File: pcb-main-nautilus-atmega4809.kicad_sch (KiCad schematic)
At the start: 11 parts, among them J1 694106301002, J2 105017-0001, J3 FTSH-105-01-L-DV-007-K, J4 AVR-UPDI-6, J5 Conn_01x06, J6 Conn_01x10, J7 Conn_01x08, J8 Conn_01x08

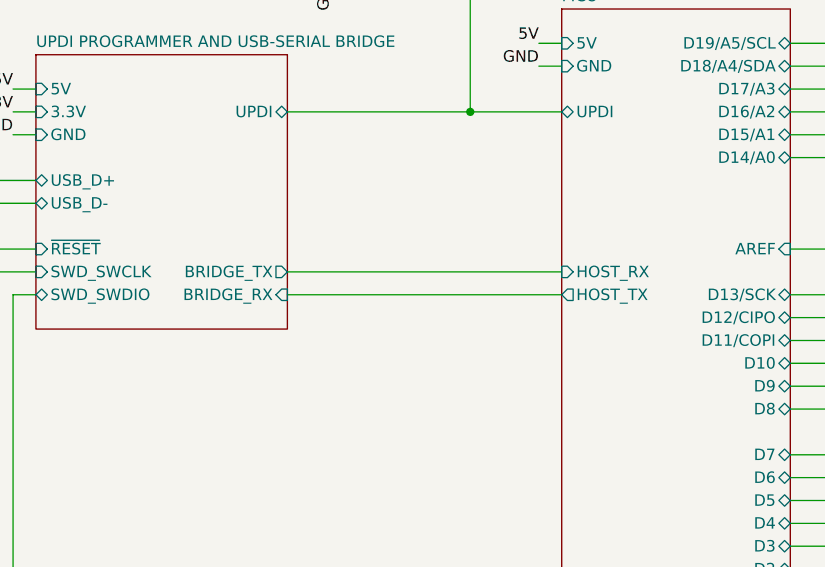
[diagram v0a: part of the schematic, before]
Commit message: Rename serial signals
Supports #2.
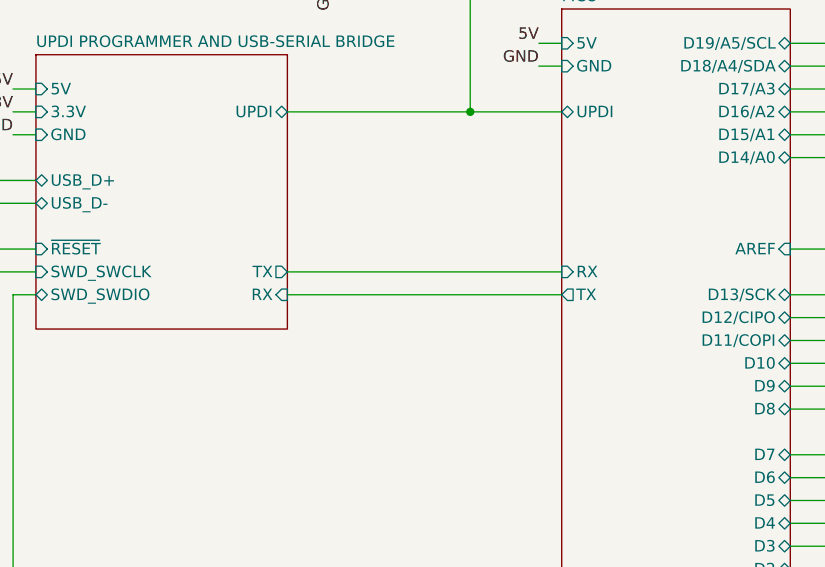
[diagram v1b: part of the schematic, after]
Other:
- sheet MCU ports: added RX, TX; removed HOST_RX, HOST_TX
- sheet UPDI PROGRAMMER AND USB-SERIAL BRIDGE ports: added RX, TX; removed BRIDGE_RX, BRIDGE_TX
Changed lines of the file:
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@@
       (effects (font (size 1.27 1.27)) (justify left))
     )
-    (pin "HOST_RX" input (at 177.8 96.52 180)
+    (pin "RX" input (at 177.8 96.52 180)
       (effects (font (size 1.27 1.27)) (justify left))
     )
-    (pin "HOST_TX" output (at 177.8 99.06 180)
+    (pin "TX" output (at 177.8 99.06 180)
       (effects (font (size 1.27 1.27)) (justify left))
     )
@@
       (effects (font (size 1.27 1.27)) (justify left))
     )
-    (pin "BRIDGE_RX" input (at 147.32 99.06 0)
+    (pin "RX" input (at 147.32 99.06 0)
       (effects (font (size 1.27 1.27)) (justify right))
     )
-    (pin "BRIDGE_TX" output (at 147.32 96.52 0)
+    (pin "TX" output (at 147.32 96.52 0)
       (effects (font (size 1.27 1.27)) (justify right))
     )

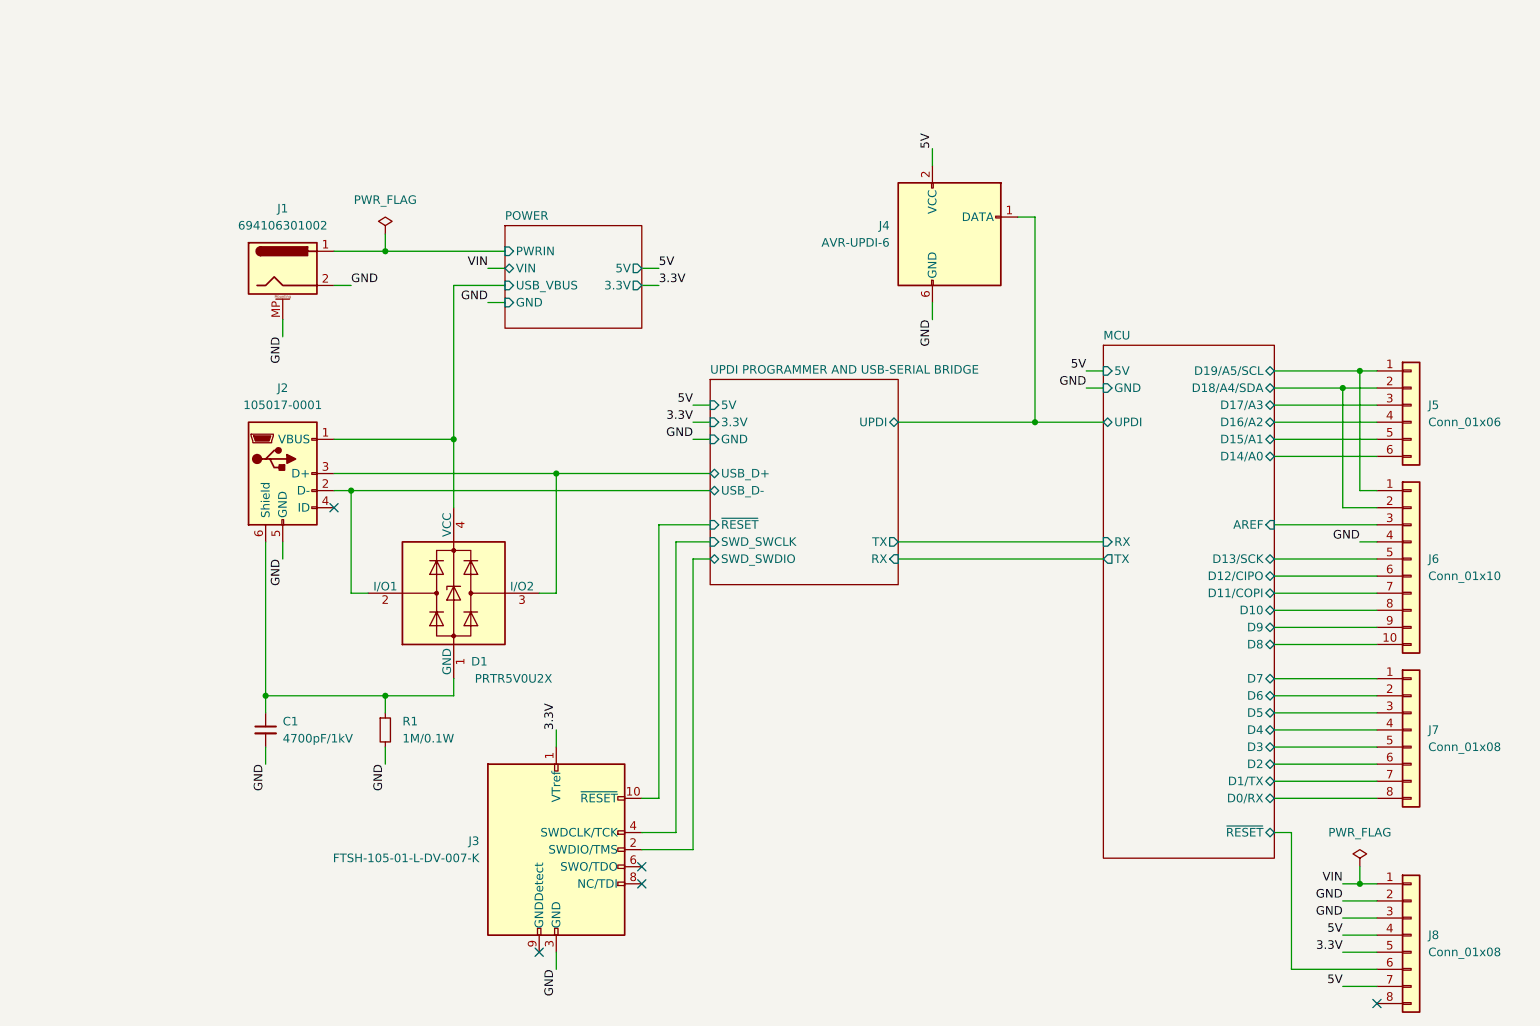
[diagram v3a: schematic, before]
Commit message: Update BOM
Supports #2.
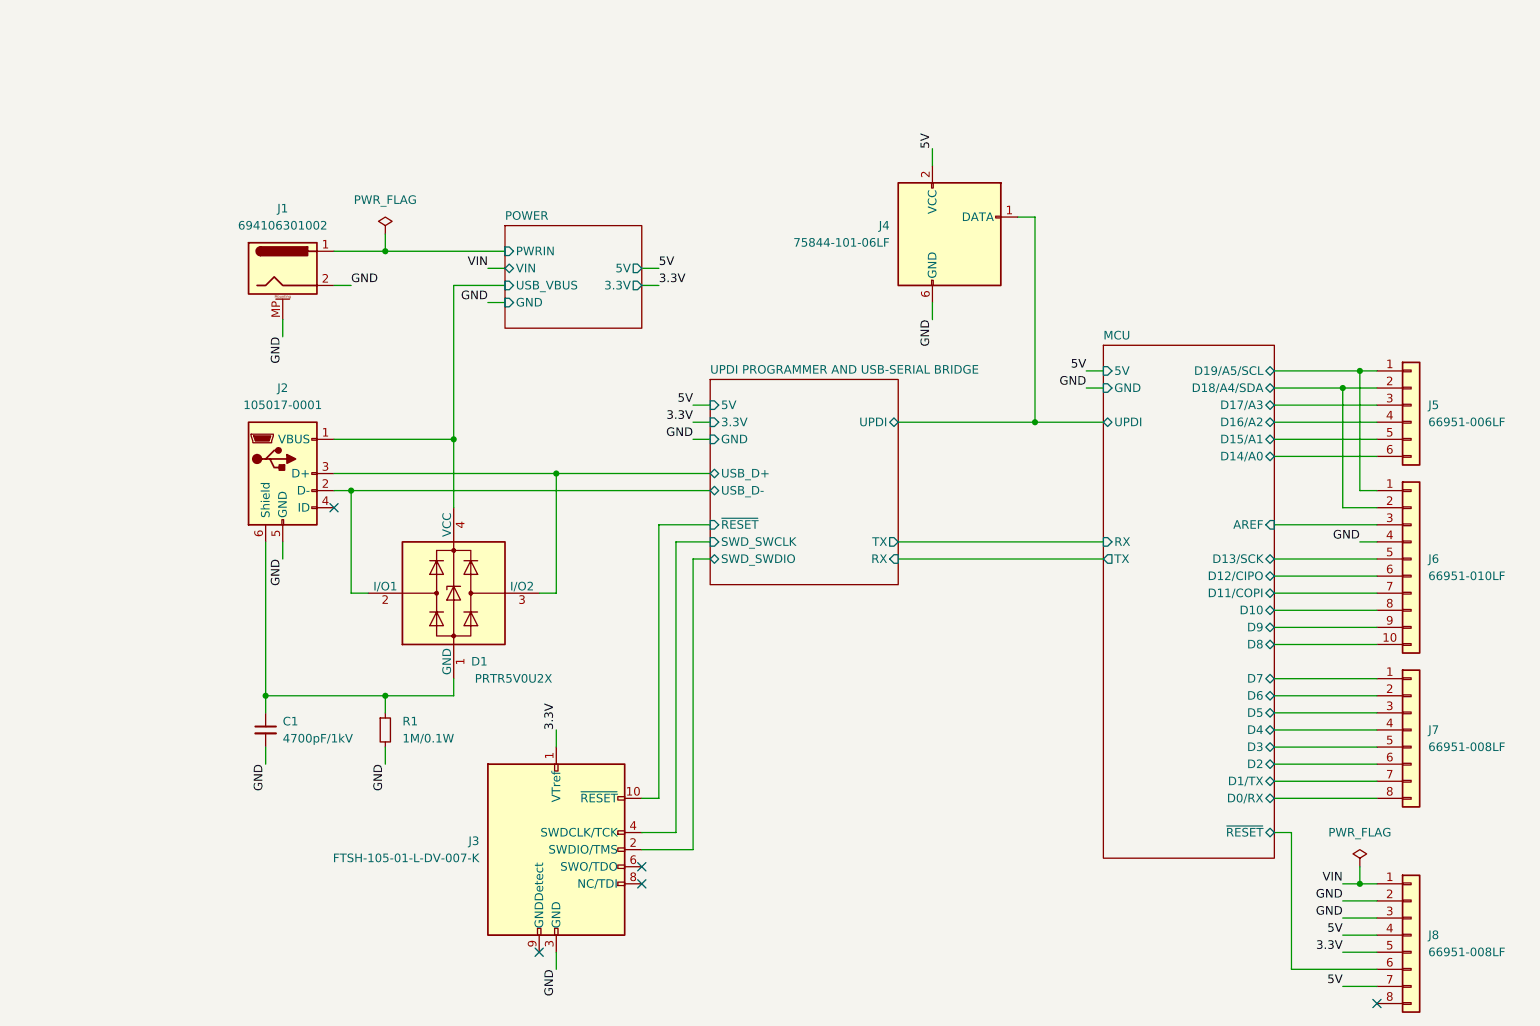
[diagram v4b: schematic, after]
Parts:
- C1: Manufacturer Part Number C0805V472KDRAC7800 -> C0805V472KDRAC
- D1: Manufacturer Part Number PRTR5V0U2X,215 -> PRTR5V0U2X
- J4: value AVR-UPDI-6 -> 75844-101-06LF; Digi-Key Part Number (none) -> 609-75844-101-06LF-ND; Manufacturer (none) -> Amphenol ICC (FCI); Manufacturer Part Number (none) -> 75844-101-06LF; Mouser Part Number (none) -> 649-75844-101-06LF
- J5: value Conn_01x06 -> 66951-006LF; Digi-Key Part Number (none) -> 609-2236-ND; Manufacturer (none) -> Amphenol ICC (FCI); Manufacturer Part Number (none) -> 66951-006LF; Mouser Part Number (none) -> 649-66951-006LF
- J6: value Conn_01x10 -> 66951-010LF; Digi-Key Part Number (none) -> 609-2240-ND; Manufacturer (none) -> Amphenol ICC (FCI); Manufacturer Part Number (none) -> 66951-010LF; Mouser Part Number (none) -> 649-66951-010LF
- J7, J8: value Conn_01x08 -> 66951-008LF; Digi-Key Part Number (none) -> 609-2238-ND; Manufacturer (none) -> Amphenol ICC (FCI); Manufacturer Part Number (none) -> 66951-008LF; Mouser Part Number (none) -> 649-66951-008LF
- R1: Manufacturer Part Number ERJ-3EKF1004V -> ERJ-3EKF1004
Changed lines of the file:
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@@
       (effects (font (size 1.27 1.27)) hide)
     )
-    (property "Manufacturer Part Number" "PRTR5V0U2X,215" (id 5) (at 81.28 104.14 0)
+    (property "Manufacturer Part Number" "PRTR5V0U2X" (id 5) (at 81.28 104.14 0)
       (effects (font (size 1.27 1.27)) hide)
     )
@@
       (effects (font (size 1.27 1.27)) (justify left))
     )
-    (property "Value" "Conn_01x08" (id 1) (at 226.06 126.9999 0)
+    (property "Value" "66951-008LF" (id 1) (at 226.06 126.9999 0)
       (effects (font (size 1.27 1.27)) (justify left))
     )
@@
       (effects (font (size 1.27 1.27)) hide)
     )
-    (property "Datasheet" "~" (id 3) (at 223.52 124.46 0)
+    (property "Datasheet" "https://cdn.amphenol-cs.com/media/wysiwyg/files/drawing/66951.pdf" (id 3) (at 223.52 124.46 0)
+      (effects (font (size 1.27 1.27)) hide)
+    )
+    (property "Manufacturer" "Amphenol ICC (FCI)" (id 4) (at 223.52 124.46 0)
+      (effects (font (size 1.27 1.27)) hide)
+    )
+    (property "Manufacturer Part Number" "66951-008LF" (id 5) (at 223.52 124.46 0)
+      (effects (font (size 1.27 1.27)) hide)
+    )
+    (property "Digi-Key Part Number" "609-2238-ND" (id 6) (at 223.52 124.46 0)
+      (effects (font (size 1.27 1.27)) hide)
+    )
+    (property "Mouser Part Number" "649-66951-008LF" (id 7) (at 223.52 124.46 0)
       (effects (font (size 1.27 1.27)) hide)
     )
@@
       (effects (font (size 1.27 1.27)) hide)
     )
-    (property "Manufacturer Part Number" "C0805V472KDRAC7800" (id 5) (at 53.34 124.46 0)
+    (property "Manufacturer Part Number" "C0805V472KDRAC" (id 5) (at 53.34 124.46 0)
       (effects (font (size 1.27 1.27)) hide)
     )
@@
       (effects (font (size 1.27 1.27)) hide)
     )
-    (property "Manufacturer Part Number" "ERJ-3EKF1004V" (id 5) (at 71.12 124.46 0)
+    (property "Manufacturer Part Number" "ERJ-3EKF1004" (id 5) (at 71.12 124.46 0)
       (effects (font (size 1.27 1.27)) hide)
     )
@@
       (effects (font (size 1.27 1.27)) (justify left))
     )
-    (property "Value" "Conn_01x10" (id 1) (at 226.06 101.5999 0)
+    (property "Value" "66951-010LF" (id 1) (at 226.06 101.5999 0)
       (effects (font (size 1.27 1.27)) (justify left))
     )
@@
       (effects (font (size 1.27 1.27)) hide)
     )
-    (property "Datasheet" "~" (id 3) (at 223.52 99.06 0)
+    (property "Datasheet" "https://cdn.amphenol-cs.com/media/wysiwyg/files/drawing/66951.pdf" (id 3) (at 223.52 99.06 0)
+      (effects (font (size 1.27 1.27)) hide)
+    )
+    (property "Manufacturer" "Amphenol ICC (FCI)" (id 4) (at 223.52 99.06 0)
+      (effects (font (size 1.27 1.27)) hide)
+    )
+    (property "Manufacturer Part Number" "66951-010LF" (id 5) (at 223.52 99.06 0)
+      (effects (font (size 1.27 1.27)) hide)
+    )
+    (property "Digi-Key Part Number" "609-2240-ND" (id 6) (at 223.52 99.06 0)
+      (effects (font (size 1.27 1.27)) hide)
+    )
+    (property "Mouser Part Number" "649-66951-010LF" (id 7) (at 223.52 99.06 0)
       (effects (font (size 1.27 1.27)) hide)
     )
@@
       (effects (font (size 1.27 1.27)) (justify left))
     )
-    (property "Value" "Conn_01x08" (id 1) (at 226.06 157.4799 0)
+    (property "Value" "66951-008LF" (id 1) (at 226.06 157.4799 0)
       (effects (font (size 1.27 1.27)) (justify left))
     )
@@
       (effects (font (size 1.27 1.27)) hide)
     )
-    (property "Datasheet" "~" (id 3) (at 223.52 154.94 0)
+    (property "Datasheet" "https://cdn.amphenol-cs.com/media/wysiwyg/files/drawing/66951.pdf" (id 3) (at 223.52 154.94 0)
+      (effects (font (size 1.27 1.27)) hide)
+    )
+    (property "Manufacturer" "Amphenol ICC (FCI)" (id 4) (at 223.52 154.94 0)
+      (effects (font (size 1.27 1.27)) hide)
+    )
+    (property "Manufacturer Part Number" "66951-008LF" (id 5) (at 223.52 154.94 0)
+      (effects (font (size 1.27 1.27)) hide)
+    )
+    (property "Digi-Key Part Number" "609-2238-ND" (id 6) (at 223.52 154.94 0)
+      (effects (font (size 1.27 1.27)) hide)
+    )
+    (property "Mouser Part Number" "649-66951-008LF" (id 7) (at 223.52 154.94 0)
       (effects (font (size 1.27 1.27)) hide)
     )
@@
       (effects (font (size 1.27 1.27)) hide)
     )
-    (property "Datasheet" "http://infocenter.arm.com/help/topic/com.arm.doc.ddi0314h/DDI0314H_coresight_components_trm.pdf" (id 3) (at 87.63 173.99 90)
+    (property "Datasheet" "https://suddendocs.samtec.com/catalog_english/ftsh_smt.pdf" (id 3) (at 87.63 173.99 90)
       (effects (font (size 1.27 1.27)) hide)
     )
@@
       (effects (font (size 1.27 1.27)) (justify right))
     )
-    (property "Value" "AVR-UPDI-6" (id 1) (at 146.05 52.0699 0)
+    (property "Value" "75844-101-06LF" (id 1) (at 146.05 52.0699 0)
       (effects (font (size 1.27 1.27)) (justify right))
     )
@@
       (effects (font (size 1.27 1.27)) hide)
     )
-    (property "Datasheet" "https://www.microchip.com/webdoc/GUID-9D10622A-5C16-4405-B092-1BDD437B4976/index.html?GUID-9B349315-2842-4189-B88C-49F4E1055D7F" (id 3) (at 122.555 64.77 0)
+    (property "Datasheet" "https://cdn.amphenol-cs.com/media/wysiwyg/files/drawing/75844.pdf" (id 3) (at 122.555 64.77 0)
+      (effects (font (size 1.27 1.27)) hide)
+    )
+    (property "Manufacturer" "Amphenol ICC (FCI)" (id 4) (at 154.94 50.8 0)
+      (effects (font (size 1.27 1.27)) hide)
+    )
+    (property "Manufacturer Part Number" "75844-101-06LF" (id 5) (at 154.94 50.8 0)
+      (effects (font (size 1.27 1.27)) hide)
+    )
+    (property "Digi-Key Part Number" "609-75844-101-06LF-ND" (id 6) (at 154.94 50.8 0)
+      (effects (font (size 1.27 1.27)) hide)
+    )
+    (property "Mouser Part Number" "649-75844-101-06LF" (id 7) (at 154.94 50.8 0)
       (effects (font (size 1.27 1.27)) hide)
     )
@@
       (effects (font (size 1.27 1.27)) (justify left))
     )
-    (property "Value" "Conn_01x06" (id 1) (at 226.06 78.7399 0)
+    (property "Value" "66951-006LF" (id 1) (at 226.06 78.7399 0)
       (effects (font (size 1.27 1.27)) (justify left))
     )
@@
       (effects (font (size 1.27 1.27)) hide)
     )
-    (property "Datasheet" "~" (id 3) (at 223.52 76.2 0)
+    (property "Datasheet" "https://cdn.amphenol-cs.com/media/wysiwyg/files/drawing/66951.pdf" (id 3) (at 223.52 76.2 0)
+      (effects (font (size 1.27 1.27)) hide)
+    )
+    (property "Manufacturer" "Amphenol ICC (FCI)" (id 4) (at 223.52 76.2 0)
+      (effects (font (size 1.27 1.27)) hide)
+    )
+    (property "Manufacturer Part Number" "66951-006LF" (id 5) (at 223.52 76.2 0)
+      (effects (font (size 1.27 1.27)) hide)
+    )
+    (property "Digi-Key Part Number" "609-2236-ND" (id 6) (at 223.52 76.2 0)
+      (effects (font (size 1.27 1.27)) hide)
+    )
+    (property "Mouser Part Number" "649-66951-006LF" (id 7) (at 223.52 76.2 0)
       (effects (font (size 1.27 1.27)) hide)
     )
@@
     )
     (path "/a762f87e-f18f-4806-abfa-7af92d8a4cc5"
-      (reference "J4") (unit 1) (value "AVR-UPDI-6") (footprint "Connector_PinHeader_2.54mm:PinHeader_2x03_P2.54mm_Vertical")
+      (reference "J4") (unit 1) (value "75844-101-06LF") (footprint "Connector_PinHeader_2.54mm:PinHeader_2x03_P2.54mm_Vertical")
     )
     (path "/fc4d2fb0-0c76-42ed-93b0-5494ded56c99"
-      (reference "J5") (unit 1) (value "Conn_01x06") (footprint "Connector_PinHeader_2.54mm:PinHeader_1x06_P2.54mm_Vertical")
+      (reference "J5") (unit 1) (value "66951-006LF") (footprint "Connector_PinHeader_2.54mm:PinHeader_1x06_P2.54mm_Vertical")
     )
     (path "/7e8ccd1c-1c23-465e-a76d-7a1689ced81a"
-      (reference "J6") (unit 1) (value "Conn_01x10") (footprint "Connector_PinHeader_2.54mm:PinHeader_1x10_P2.54mm_Vertical")
+      (reference "J6") (unit 1) (value "66951-010LF") (footprint "Connector_PinHeader_2.54mm:PinHeader_1x10_P2.54mm_Vertical")
     )
     (path "/1861d396-eaf2-4961-adae-c4aecc6209ef"
-      (reference "J7") (unit 1) (value "Conn_01x08") (footprint "Connector_PinHeader_2.54mm:PinHeader_1x08_P2.54mm_Vertical")
+      (reference "J7") (unit 1) (value "66951-008LF") (footprint "Connector_PinHeader_2.54mm:PinHeader_1x08_P2.54mm_Vertical")
     )
     (path "/87af8cfd-fe1b-4ff4-bd02-ccb4e2f53955"
-      (reference "J8") (unit 1) (value "Conn_01x08") (footprint "Connector_PinHeader_2.54mm:PinHeader_1x08_P2.54mm_Vertical")
+      (reference "J8") (unit 1) (value "66951-008LF") (footprint "Connector_PinHeader_2.54mm:PinHeader_1x08_P2.54mm_Vertical")
     )
     (path "/9563730f-8d1a-4fdb-af84-834004e725da/e8c125a0-c891-462e-9bd4-251e59b83fd3"
@@
     )
     (path "/9563730f-8d1a-4fdb-af84-834004e725da/1bc06f9c-8e97-48fc-821f-17675566bdcb/faa0bcb3-92cf-49f0-8c93-d9591933f632"
-      (reference "Q1") (unit 1) (value "BSS138PW,115") (footprint "Package_TO_SOT_SMD:SOT-323_SC-70_Handsoldering")
+      (reference "Q1") (unit 1) (value "BSS138PW") (footprint "Package_TO_SOT_SMD:SOT-323_SC-70_Handsoldering")
     )
     (path "/9563730f-8d1a-4fdb-af84-834004e725da/92d71020-50e1-4f76-b15a-ae0e83f5b145/faa0bcb3-92cf-49f0-8c93-d9591933f632"
-      (reference "Q2") (unit 1) (value "BSS138PW,115") (footprint "Package_TO_SOT_SMD:SOT-323_SC-70_Handsoldering")
+      (reference "Q2") (unit 1) (value "BSS138PW") (footprint "Package_TO_SOT_SMD:SOT-323_SC-70_Handsoldering")
     )
     (path "/9563730f-8d1a-4fdb-af84-834004e725da/d987396a-6e77-4357-87d0-f98ddb7f11de/faa0bcb3-92cf-49f0-8c93-d9591933f632"
-      (reference "Q3") (unit 1) (value "BSS138PW,115") (footprint "Package_TO_SOT_SMD:SOT-323_SC-70_Handsoldering")
+      (reference "Q3") (unit 1) (value "BSS138PW") (footprint "Package_TO_SOT_SMD:SOT-323_SC-70_Handsoldering")
     )
     (path "/389d681b-46d3-41f6-9129-89b7ca7ff91f"
